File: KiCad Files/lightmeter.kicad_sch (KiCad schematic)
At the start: 23 parts, among them J1 LCD Pins, J2 BATTERY, J3 USB_C_5V_POWER, SW1 RESET_SW, U1 ATmega328P-A, U2 TP4056, U3 AMS1117-3.3, U4 DW01, U5 FS8205A, Y1 8MHz

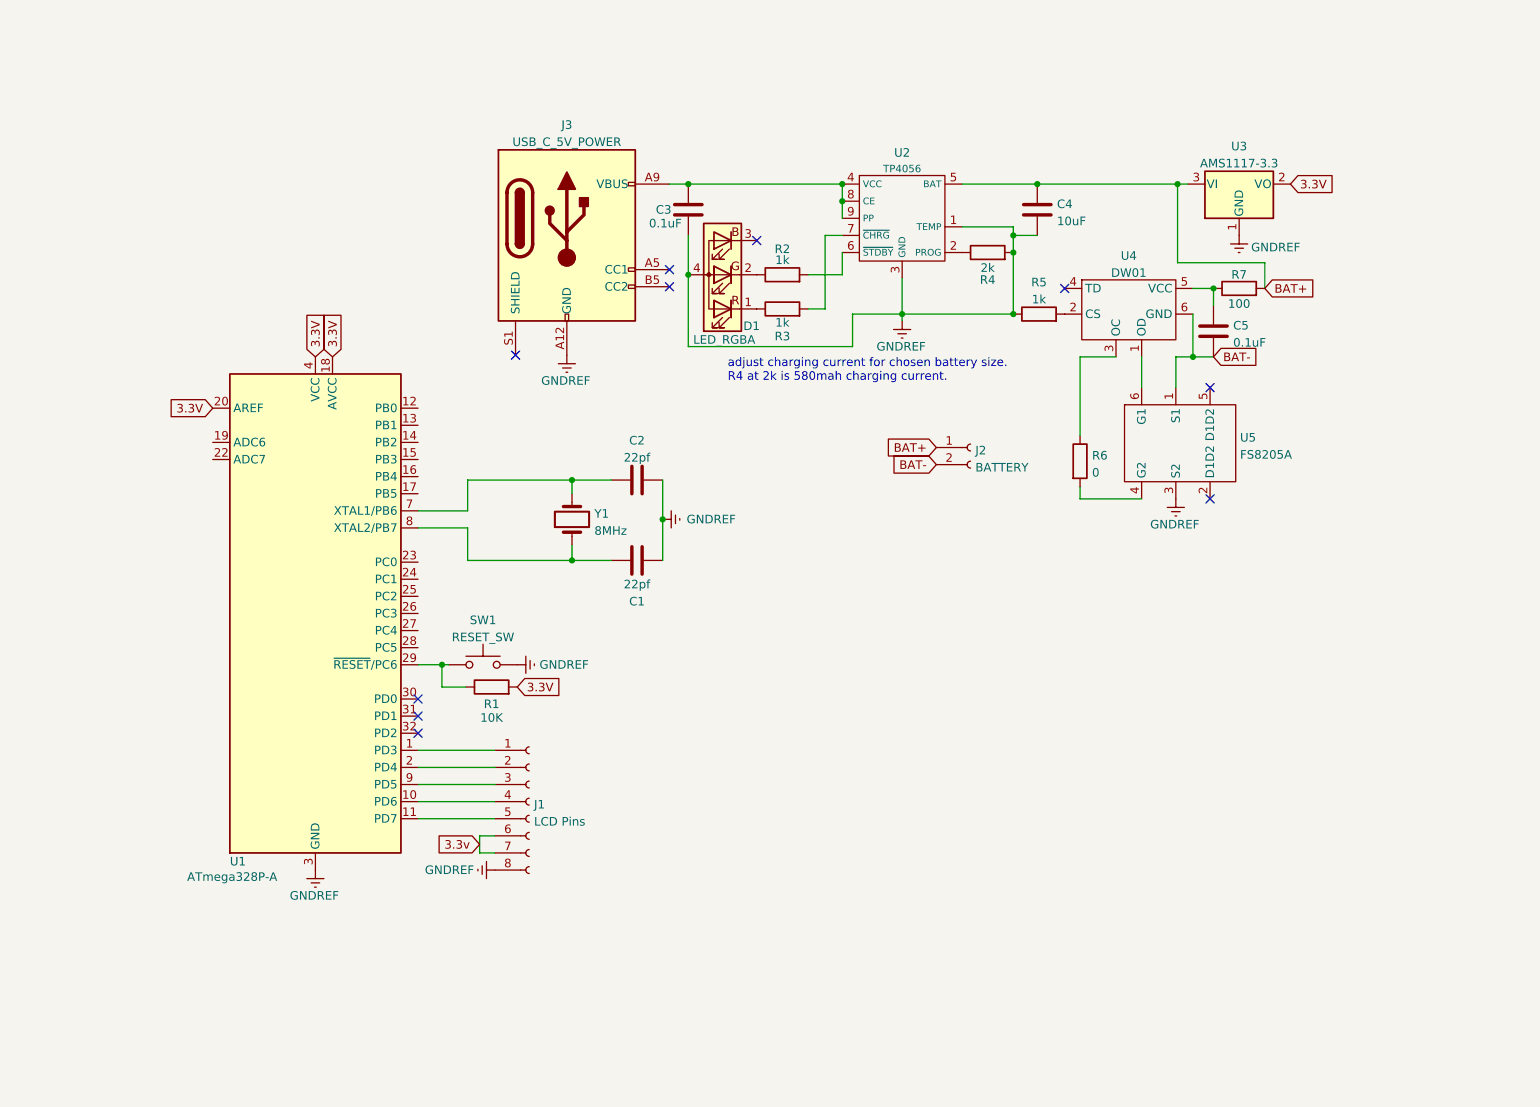
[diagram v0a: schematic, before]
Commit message: Finalized Initial Schematic.
Charging circuit is done. Navigation buttons/system works on paper.
Need to look into if the voltage divider for the battery reading would interfere with the DW01 battery protection IC.
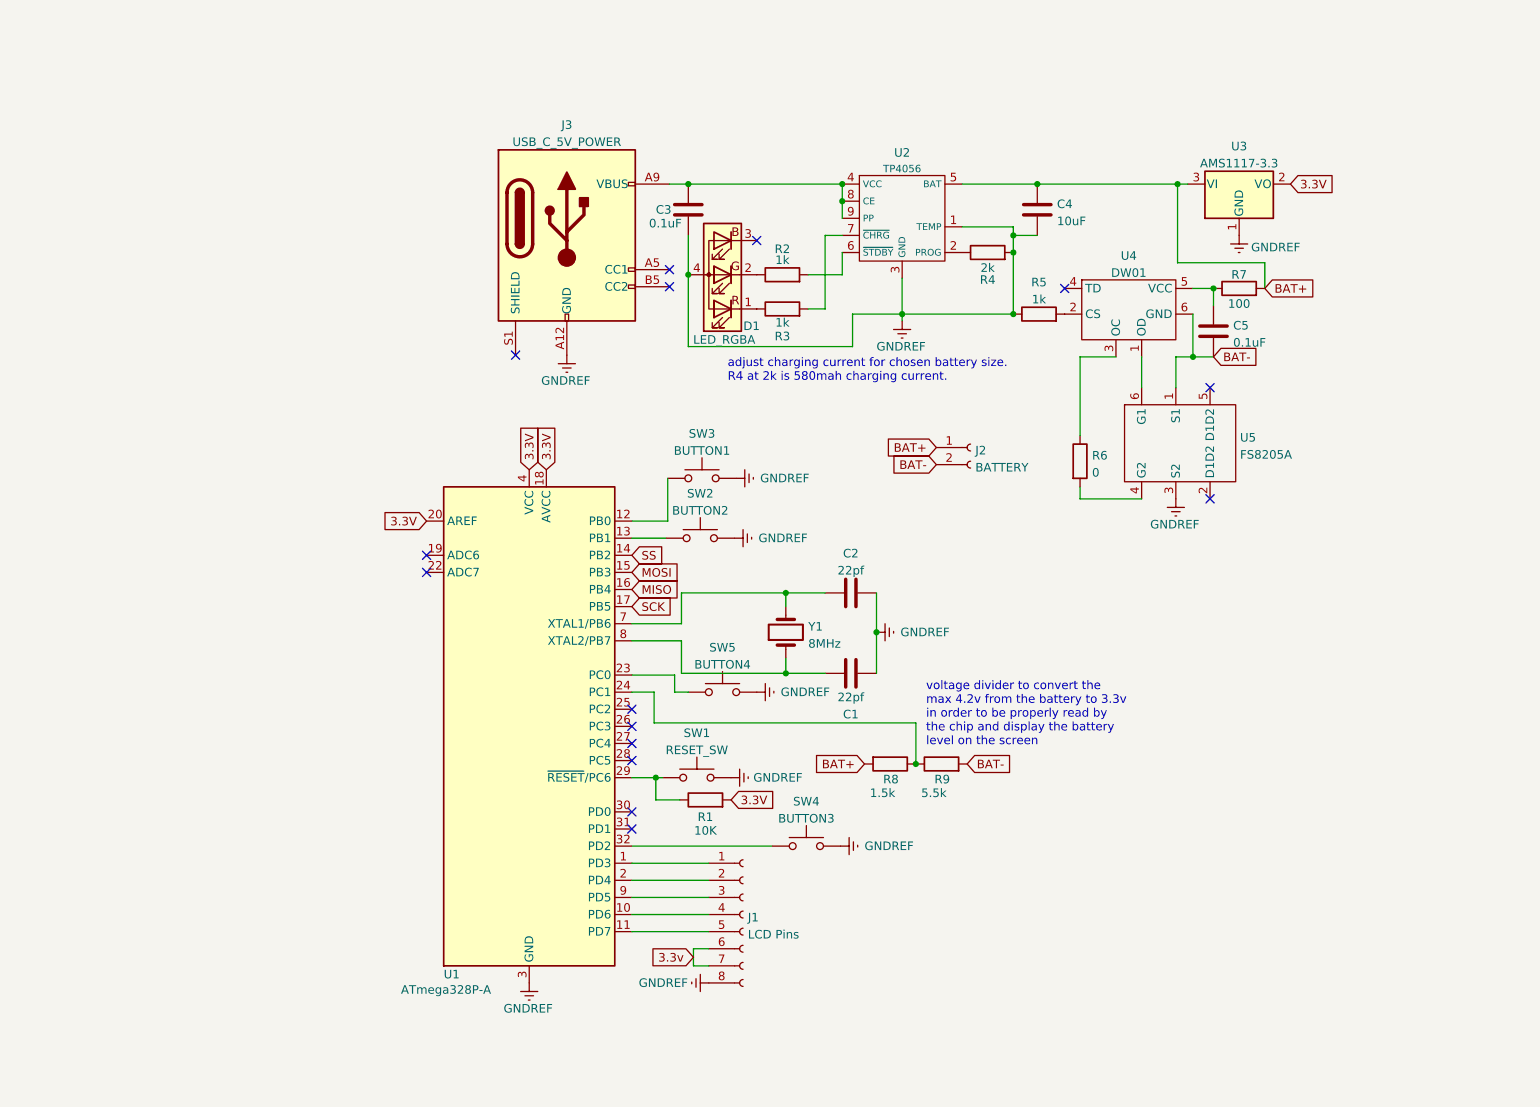
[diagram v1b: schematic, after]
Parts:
- added R8: 1.5k, symbol Device:R
- added R9: 5.5k, symbol Device:R
- added SW2: BUTTON2, symbol Switch:SW_Push
- added SW3: BUTTON1, symbol Switch:SW_Push
- added SW4: BUTTON3, symbol Switch:SW_Push
- added SW5: BUTTON4, symbol Switch:SW_Push
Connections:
- net BAT+: now also R8.2
- net BAT-: now also R9.2
- net GNDREF: now also SW2.2, SW3.2, SW4.2, SW5.2
- net at U1.12 (PB0): now also SW3.1
- net at U1.13 (PB1): now also SW2.1
- net SS: now reaches U1.14 (PB2)
- net MOSI: now reaches U1.15 (PB3)
- net MISO: now reaches U1.16 (PB4)
- net SCK: now reaches U1.17 (PB5)
- net at U1.23 (PC0): now also SW5.1
- net at U1.24 (PC1): now also R8.1, R9.1
- net at U1.32 (PD2): now also SW4.1
- no-connect marks 10 -> 15
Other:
- note added: "voltage divider to convert the max 4.2v from the battery to 3.3v in order to be properly read by the chip and display the battery level on the screen"
- moved on the sheet: C1, C2, J1, R1, SW1, U1, Y1

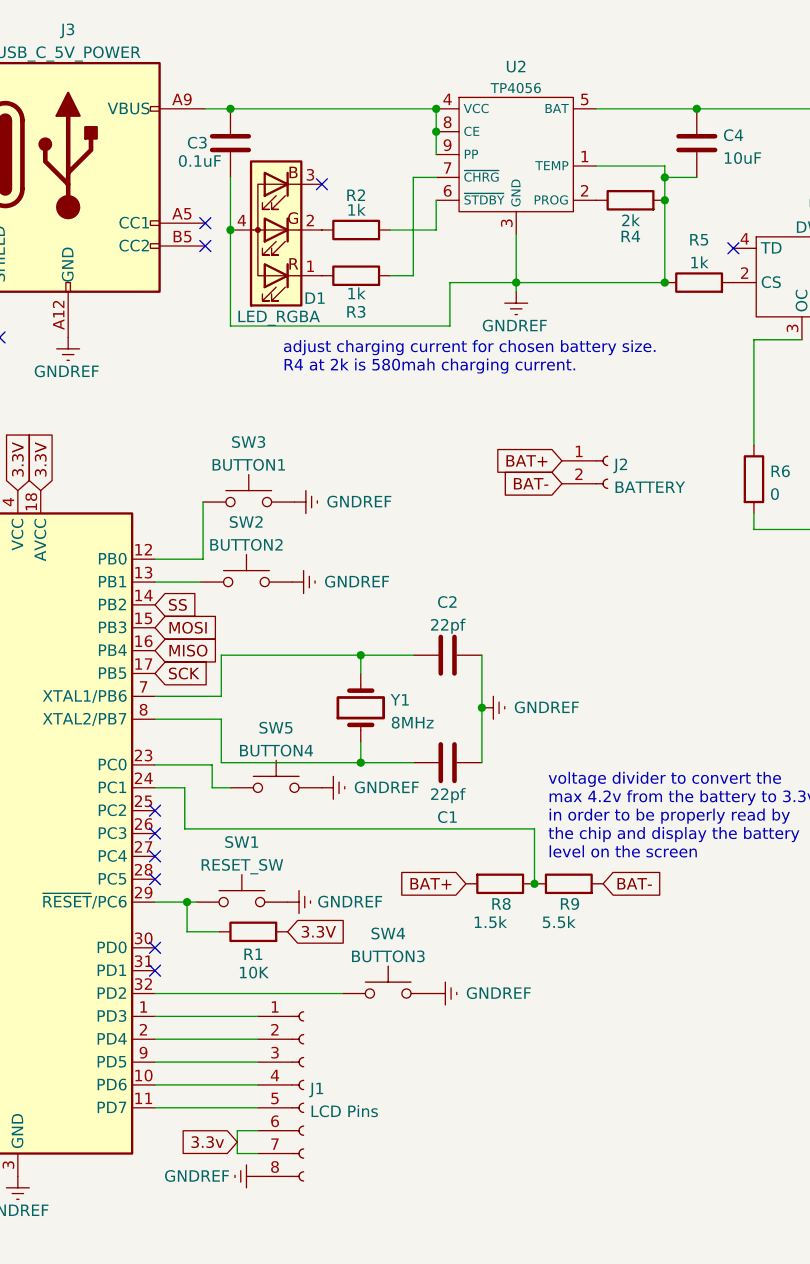
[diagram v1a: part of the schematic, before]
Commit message: Updated Schematic Slightly.
Removed the RGB LED charging indicators on the tp4056. Added pads for ICSP that I forgot.
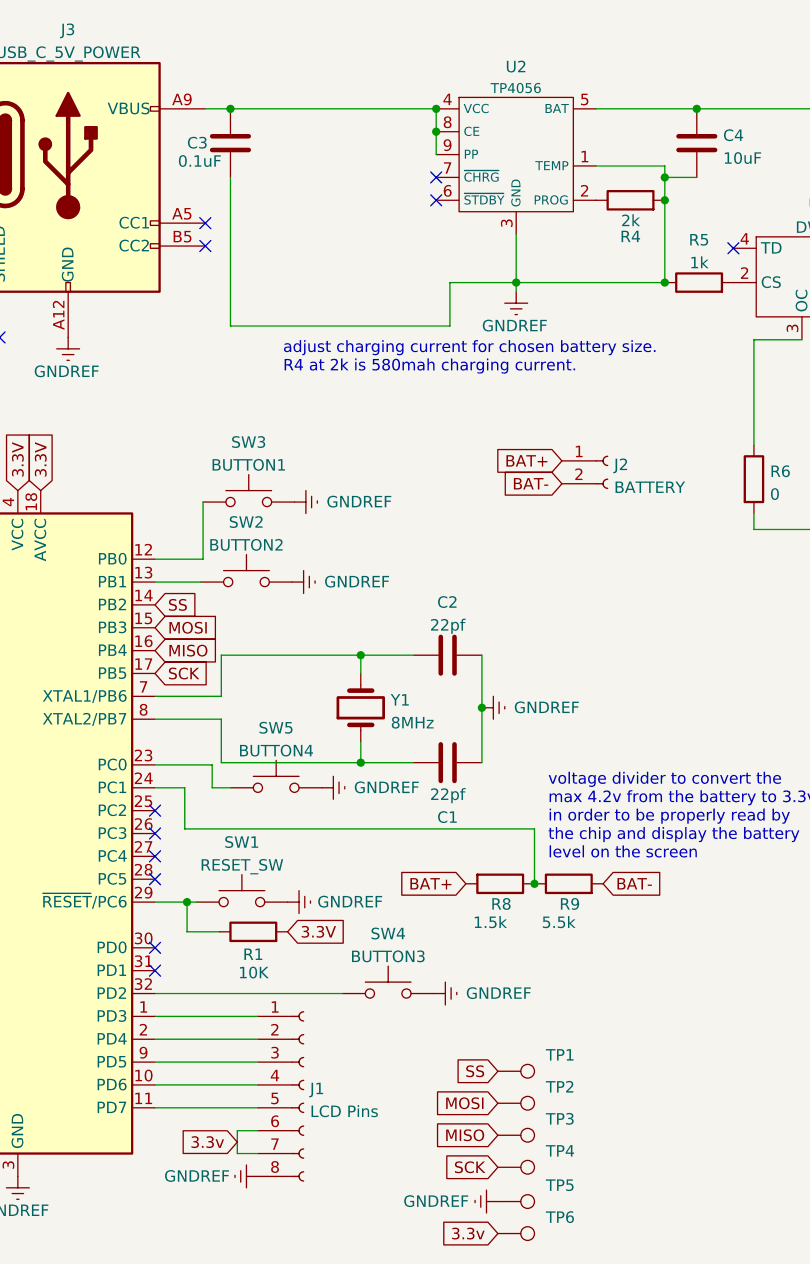
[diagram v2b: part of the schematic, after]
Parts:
- removed D1: LED_RGBA, symbol Device:LED_RGBA
- removed R2, R3: 1k, symbol Device:R
- added TP1, TP2, TP3, TP4, TP5, TP6: TestPoint, symbol Connector:TestPoint
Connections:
- net 3.3v: now also TP6.1
- net GNDREF: now also TP5.1
- net MISO: now also TP3.1
- net MOSI: now also TP2.1
- net SCK: now also TP4.1
- net SS: now also TP1.1
- no-connect marks 15 -> 16
